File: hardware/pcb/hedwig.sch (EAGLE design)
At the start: 75 parts, among them IC1 MPL3115A2LGA, J1 DX07B024JJ1R1500, P1 JTAG-10MINI, Q1 16MHz, Q2 IRLML6402, U1 NRF24L01SMD, U2 TEXAS_INSTRUMENTS_TLC59731DRT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, U3 FT232RQ, U5 ADP2302, U7 9DoF IMU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

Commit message: updated schematic and pcb
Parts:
- removed U$6: DIODE, falcon:DIODE
- removed U7: 9DoF IMU, SparkFun-Sensors:ICM-20948
- added 1.8V: TPB2,54, testpad:TPB2,54
- added C22: 47uF, SparkFun-Capacitors:4.7UF-0603-35V-(20%)
- added D3: SURS8360BT3G, falcon:DIODE
- added Q3, Q6: 20V/0.2A/8MHz/1.2Ω/1Vth, SparkFun-DiscreteSemi:MOSFET-NCH-RE1C002UN
- added R11, R8: 5.1k, SparkFun-Resistors:5.1KOHM5.1KOHM-0603-1/10W-1%
- added R12, R14: 2.49k, SparkFun-Resistors:2.49KOHM-0603-1/10W-1%
- added U4: TPS7A26-1.8, falcon:TPS7A26-1.8
- added U6: 9DoF IMU, SparkFun-Sensors:ICM-20948
- C10, C11: value 1.5pF -> 0.1uF
- C14: value 2.2uF -> 0.1uF
- C17: value 100nF -> 0.1uF
- C8, C9: value 8.2pF -> 0.1uF
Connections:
- new net 1P8V: 1.8V.TP, C16.1, Q3.G, Q6.G, R12.2, R14.2, U4.OUT, U6.!CS, U6.VDD
- new net N$15: J1.CC2, R8.2
- new net N$26: J1.CC1, R11.2
- new net SENSOR_SCL_LV: Q6.S, R14.1, U6.SCL/SCLK
- new net SENSOR_SDA_LV: Q3.S, R12.1, U6.SDA/SDI
- net +3V3: now also C22.1, U4.EN, U4.IN; no longer C16.1, U7.!CS, U7.VDD
- net +5V: now also D3.C; no longer U$6.C
- net ADSD_STUB: now also U6.AD0/SDO; no longer U7.AD0/SDO
- net GND: now also C22.2, R11.1, R8.1, U4.GND, U4.PG, U6.GND; no longer U7.GND
- net REGOUT: now also U6.REGOUT; no longer U7.REGOUT
- net SENSOR_SCL: now also Q6.D; no longer U7.SCL/SCLK
- net SENSOR_SDA: now also Q3.D; no longer U7.SDA/SDI
- net USB_VCC: now also D3.A; no longer U$6.A
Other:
- note added: "3.3V to 1.8V Conversion"
- note added: "5V to 3.3V Conversion"
- note added: "Barometer"
- note added: "IMU"
- note added: "IMU I2C Voltage Shifters"
- note added: "LED Driver"
- note added: "Outputs and Input Selection"
- note added: "Reset Button"

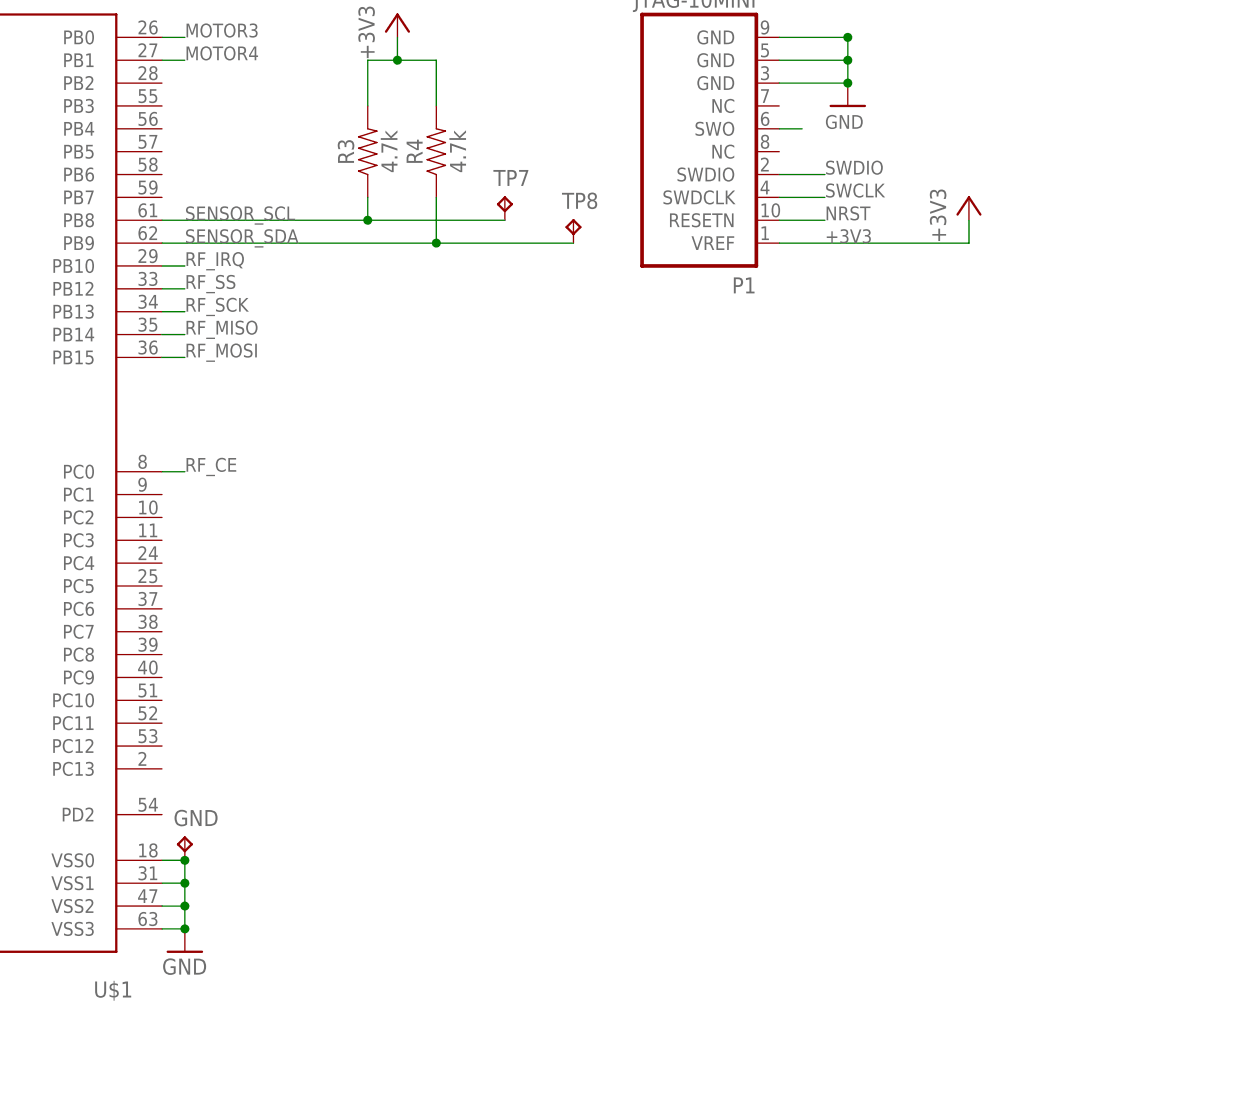
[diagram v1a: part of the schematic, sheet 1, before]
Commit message: change top plane to gnd and add breakout
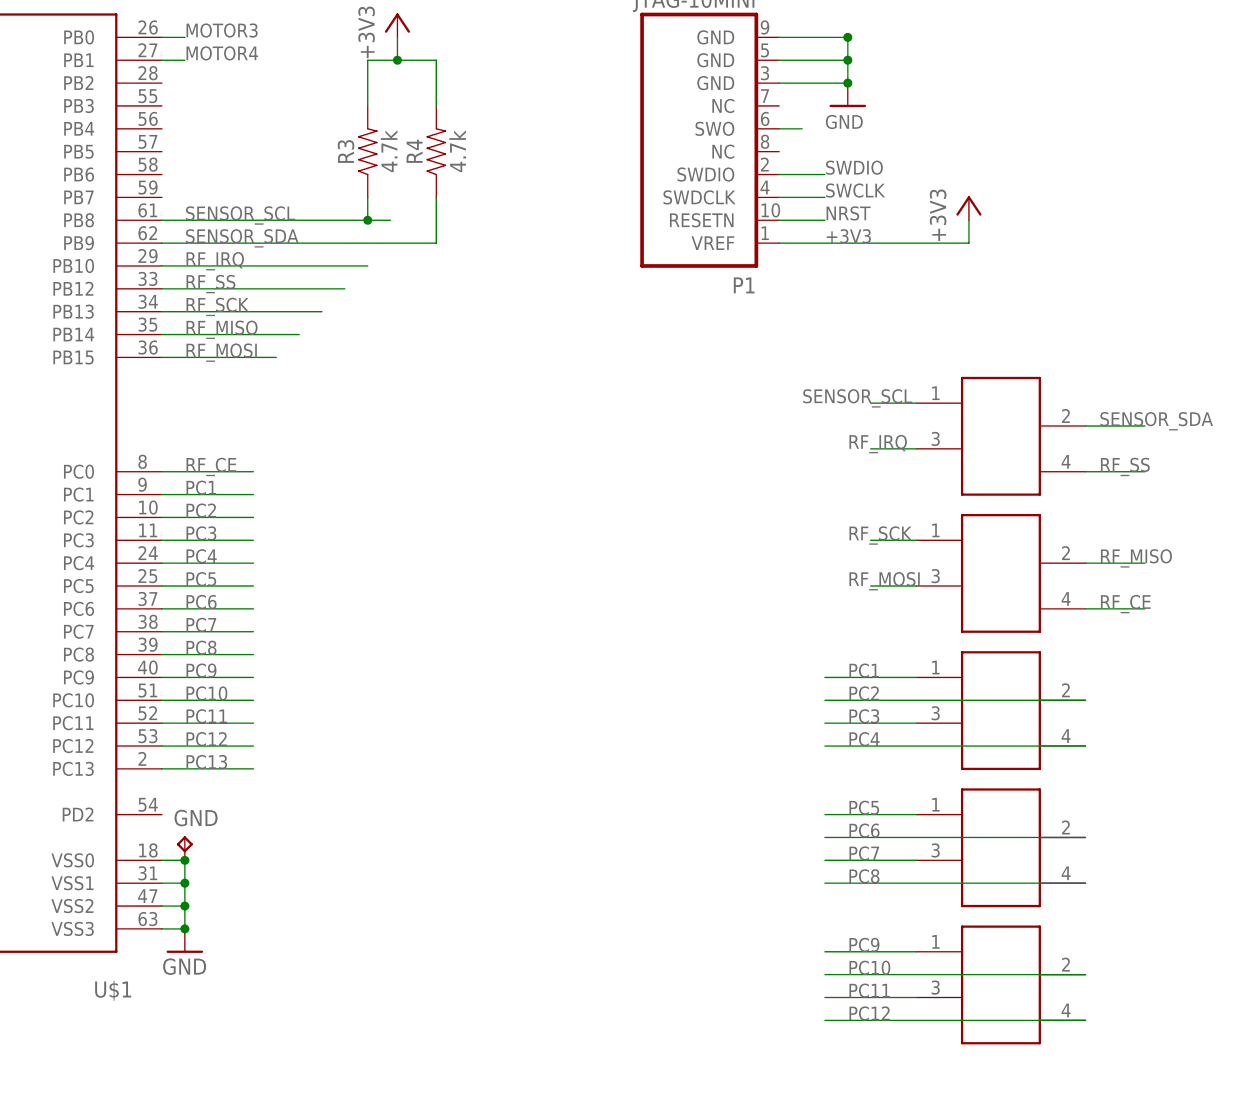
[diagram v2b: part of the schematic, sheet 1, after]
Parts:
- removed TP1, TP2, TP3, TP4, TP5, TP6, TP7, TP8: TPB1,27, testpad:TPB1,27
- added P2: SENSOR_SCL, falcon:STAG_CONN
- added P3: RF_SCK, falcon:STAG_CONN
- added P4: PC1, falcon:STAG_CONN
- added P5: PC5, falcon:STAG_CONN
- added P6: PC9, falcon:STAG_CONN
- renumbered 5V_BAT1 to 5V_BAT, GND_BAT1 to GND_BAT
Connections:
- new net PC1: P4.@1, U$1.PC1
- new net PC10: P6.@2, U$1.PC10
- new net PC11: P6.@3, U$1.PC11
- new net PC12: P6.@4, U$1.PC12
- new net PC13: U$1.PC13
- new net PC2: P4.@2, U$1.PC2
- new net PC3: P4.@3, U$1.PC3
- new net PC4: P4.@4, U$1.PC4
- new net PC5: P5.@1, U$1.PC5
- new net PC6: P5.@2, U$1.PC6
- new net PC7: P5.@3, U$1.PC7
- new net PC8: P5.@4, U$1.PC8
- new net PC9: P6.@1, U$1.PC9
- net RF_CE: now also P3.@4; no longer TP1.TP
- net RF_IRQ: now also P2.@3; no longer TP6.TP
- net RF_MISO: now also P3.@2; no longer TP5.TP
- net RF_MOSI: now also P3.@3; no longer TP4.TP
- net RF_SCK: now also P3.@1; no longer TP3.TP
- net RF_SS: now also P2.@4; no longer TP2.TP
- net SENSOR_SCL: now also P2.@1; no longer TP7.TP
- net SENSOR_SDA: now also P2.@2; no longer TP8.TP

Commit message: newest version - done
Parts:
- added C23: 47uF, SparkFun-Capacitors:4.7UF-0603-35V-(20%)
- added C24, C25: 0.1uF, SparkFun-Capacitors:0.22UF-0603-25V-10%
- added C26, C27, C28: 0.1uF, SparkFun-Capacitors:0.1UF-0603-25V-(+80/-20%)
- renumbered IC1 to U7
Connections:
- removed net 1P8V: 1.8V.TP, C16.1, Q3.G, Q6.G, R12.2, R14.2, U4.OUT, U6.!CS, U6.VDD
- new net 1V8: 1.8V.TP, C16.1, C23.1, Q3.G, Q6.G, R12.2, R14.2, U4.OUT, U6.!CS, U6.VDD, U6.VDDIO
- net +3V3: now also C24.1, C25.1, C26.2, C27.2, C28.2
- net GND: now also C23.2, C24.2, C25.2, C26.1, C27.1, C28.1
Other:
- note added: "Breakout Pins"
- note added: "Debug Out"
- note added: "NRF24L01 Radio"
- note added: "STM32F412"
- note added: "USB C Connector and FTDI"
- moved on the sheet: J1, JP1, P1, R11, R8, USB_VCC

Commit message: Pcb overhall - put imu in middle, made board square
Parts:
- removed C25: 0.1uF, SparkFun-Capacitors:0.22UF-0603-25V-10%
- removed R6: 470, SparkFun-Resistors:1.5KOHM-0603-1/10W-1%
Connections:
- net +3V3: no longer C25.1, R6.2
- net GND: no longer C25.2
- net N$16: no longer R6.1
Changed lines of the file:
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@@
 <part name="GND14" library="supply1" library_urn="urn:adsk.eagle:library:371" deviceset="GND" device=""/>
 <part name="R5" library="SparkFun-Resistors" deviceset="1.5KOHM" device="-0603-1/10W-1%" value="470"/>
-<part name="+3V8" library="supply1" library_urn="urn:adsk.eagle:library:371" deviceset="+3V3" device=""/>
-<part name="R6" library="SparkFun-Resistors" deviceset="1.5KOHM" device="-0603-1/10W-1%" value="470"/>
 <part name="+3V7" library="supply1" library_urn="urn:adsk.eagle:library:371" deviceset="+3V3" device=""/>
 <part name="GND" library="testpad" library_urn="urn:adsk.eagle:library:385" deviceset="TP" device="B2,54" package3d_urn="urn:adsk.eagle:package:27948/1"/>
@@
 <part name="C23" library="SparkFun-Capacitors" deviceset="4.7UF" device="-0603-35V-(20%)" value="47uF"/>
 <part name="C24" library="SparkFun-Capacitors" deviceset="0.22UF" device="-0603-25V-10%" value="0.1uF"/>
-<part name="C25" library="SparkFun-Capacitors" deviceset="0.22UF" device="-0603-25V-10%" value="0.1uF"/>
 <part name="GND31" library="supply1" library_urn="urn:adsk.eagle:library:371" deviceset="GND" device=""/>
 <part name="C26" library="SparkFun-Capacitors" deviceset="0.1UF" device="-0603-25V-(+80/-20%)" value="0.1uF"/>
@@
 <attribute name="VALUE" x="-77.216" y="17.78" size="1.778" layer="96" font="vector" rot="R90" align="top-center"/>
 </instance>
-<instance part="+3V8" gate="G$1" x="-78.74" y="49.276" smashed="yes">
-<attribute name="VALUE" x="-81.28" y="44.196" size="1.778" layer="96" rot="R90"/>
-</instance>
-<instance part="R6" gate="G$1" x="-78.74" y="35.56" smashed="yes" rot="R90">
-<attribute name="NAME" x="-80.264" y="35.56" size="1.778" layer="95" font="vector" rot="R90" align="bottom-center"/>
-<attribute name="VALUE" x="-77.216" y="35.56" size="1.778" layer="96" font="vector" rot="R90" align="top-center"/>
-</instance>
 <instance part="+3V7" gate="G$1" x="-38.1" y="67.056" smashed="yes">
 <attribute name="VALUE" x="-40.64" y="61.976" size="1.778" layer="96" rot="R90"/>
@@
 <wire x1="31.242" y1="55.88" x2="31.242" y2="53.34" width="0.1524" layer="91"/>
 <junction x="31.242" y="53.34"/>
-</segment>
-<segment>
-<pinref part="R6" gate="G$1" pin="2"/>
-<pinref part="+3V8" gate="G$1" pin="+3V3"/>
-<wire x1="-78.74" y1="40.64" x2="-78.74" y2="46.736" width="0.1524" layer="91"/>
 </segment>
 <segment>
@@
 <segment>
 <pinref part="R5" gate="G$1" pin="2"/>
-<pinref part="R6" gate="G$1" pin="1"/>
 <wire x1="-78.74" y1="22.86" x2="-78.74" y2="27.94" width="0.1524" layer="91"/>
 <pinref part="U$1" gate="G$1" pin="BOOT0"/>
-<wire x1="-78.74" y1="27.94" x2="-78.74" y2="30.48" width="0.1524" layer="91"/>
 <wire x1="-38.1" y1="27.94" x2="-78.74" y2="27.94" width="0.1524" layer="91"/>
-<junction x="-78.74" y="27.94"/>
 </segment>
 </net>
@@
 <attribute name="VALUE" x="-11.176" y="33.401" size="1.778" layer="96" font="vector"/>
 </instance>
-<instance part="C25" gate="G$1" x="-2.54" y="35.56" smashed="yes">
-<attribute name="NAME" x="-1.016" y="38.481" size="1.778" layer="95" font="vector"/>
-<attribute name="VALUE" x="-1.016" y="33.401" size="1.778" layer="96" font="vector"/>
-</instance>
 <instance part="GND31" gate="1" x="-10.16" y="30.48" smashed="yes">
 <attribute name="VALUE" x="-12.7" y="27.94" size="1.778" layer="96"/>
@@
 </segment>
 <segment>
-<pinref part="C25" gate="G$1" pin="2"/>
 <pinref part="C24" gate="G$1" pin="2"/>
-<wire x1="-2.54" y1="33.02" x2="-10.16" y2="33.02" width="0.1524" layer="91"/>
 <pinref part="GND31" gate="1" pin="GND"/>
 <wire x1="-10.16" y1="33.02" x2="-12.7" y2="33.02" width="0.1524" layer="91"/>
-<junction x="-10.16" y="33.02"/>
 </segment>
 </net>
@@
 <wire x1="-22.86" y1="40.64" x2="-12.7" y2="40.64" width="0.1524" layer="91"/>
 <junction x="-22.86" y="40.64"/>
-<pinref part="C25" gate="G$1" pin="1"/>
-<wire x1="-12.7" y1="40.64" x2="-2.54" y2="40.64" width="0.1524" layer="91"/>
-<junction x="-12.7" y="40.64"/>
-</segment>
-</net>
+</segment>
+</net>
